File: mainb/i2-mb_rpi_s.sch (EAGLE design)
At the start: 36 parts, among them IC3 DS1307Z, T1 BC337, T2 BC337, X9 eth (mb->rpi)

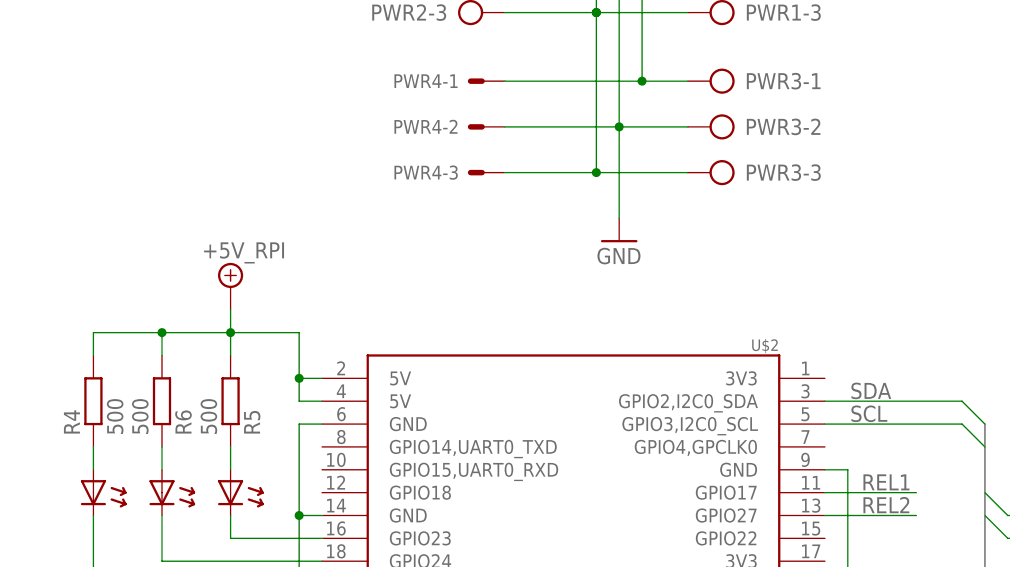
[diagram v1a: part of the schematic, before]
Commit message: mainb: 8) leds -> 3V3
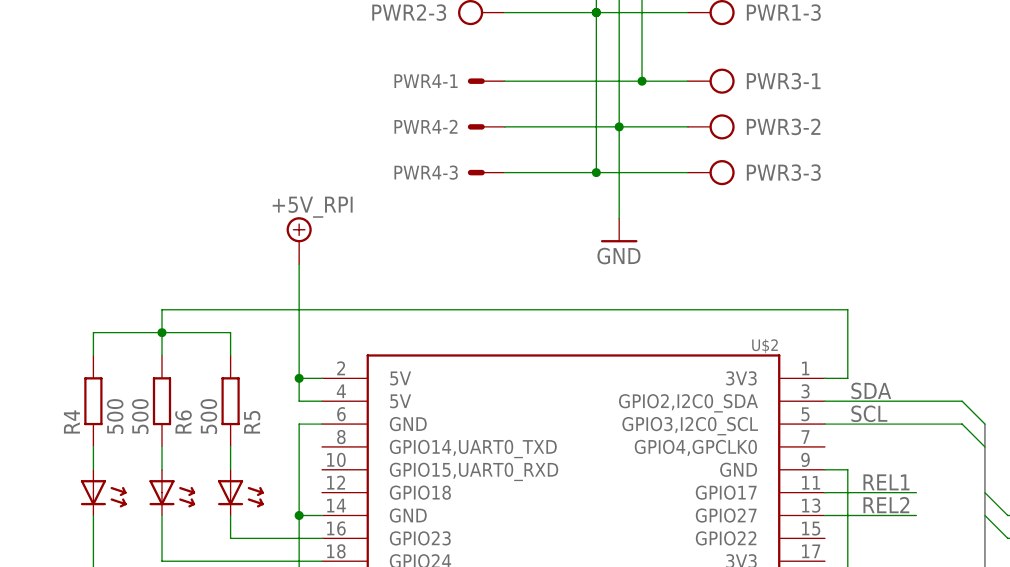
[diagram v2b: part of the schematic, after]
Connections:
- new net N$11: R4.2, R5.2, R6.2, U$2.3V3@1
- net +5V_RPI: no longer R4.2, R5.2, R6.2
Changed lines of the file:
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@@
 <instance part="X9" gate="-7" x="-182.88" y="40.64" rot="MR0"/>
 <instance part="X9" gate="-8" x="-182.88" y="38.1" rot="MR0"/>
-<instance part="SUPPLY2" gate="G$1" x="-71.12" y="20.32"/>
+<instance part="SUPPLY2" gate="G$1" x="-63.5" y="25.4"/>
 <instance part="SUPPLY3" gate="G$1" x="-91.44" y="-55.88" smashed="yes" rot="MR0">
 <attribute name="VALUE" x="-83.693" y="-52.451" size="1.778" layer="96" rot="MR0"/>
@@
 <wire x1="-60.96" y1="10.16" x2="-63.5" y2="10.16" width="0.1524" layer="91"/>
 <junction x="-63.5" y="10.16"/>
-<wire x1="-63.5" y1="10.16" x2="-63.5" y2="15.24" width="0.1524" layer="91"/>
-<wire x1="-63.5" y1="15.24" x2="-71.12" y2="15.24" width="0.1524" layer="91"/>
-<wire x1="-71.12" y1="15.24" x2="-71.12" y2="17.78" width="0.1524" layer="91"/>
+<wire x1="-63.5" y1="10.16" x2="-63.5" y2="22.86" width="0.1524" layer="91"/>
 <pinref part="SUPPLY2" gate="G$1" pin="+5V/1"/>
-<pinref part="R5" gate="G$1" pin="2"/>
-<pinref part="R6" gate="G$1" pin="2"/>
-<wire x1="-71.12" y1="12.7" x2="-71.12" y2="15.24" width="0.1524" layer="91"/>
-<wire x1="-78.74" y1="12.7" x2="-78.74" y2="15.24" width="0.1524" layer="91"/>
-<wire x1="-78.74" y1="15.24" x2="-71.12" y2="15.24" width="0.1524" layer="91"/>
-<junction x="-71.12" y="15.24"/>
-<pinref part="R4" gate="G$1" pin="2"/>
-<wire x1="-86.36" y1="12.7" x2="-86.36" y2="15.24" width="0.1524" layer="91"/>
-<wire x1="-86.36" y1="15.24" x2="-78.74" y2="15.24" width="0.1524" layer="91"/>
-<junction x="-78.74" y="15.24"/>
 </segment>
 <segment>
@@
 </segment>
 </net>
+<net name="N$11" class="0">
+<segment>
+<pinref part="R6" gate="G$1" pin="2"/>
+<wire x1="-78.74" y1="12.7" x2="-78.74" y2="15.24" width="0.1524" layer="91"/>
+<pinref part="R4" gate="G$1" pin="2"/>
+<wire x1="-86.36" y1="12.7" x2="-86.36" y2="15.24" width="0.1524" layer="91"/>
+<wire x1="-86.36" y1="15.24" x2="-78.74" y2="15.24" width="0.1524" layer="91"/>
+<pinref part="R5" gate="G$1" pin="2"/>
+<wire x1="-78.74" y1="15.24" x2="-71.12" y2="15.24" width="0.1524" layer="91"/>
+<wire x1="-71.12" y1="15.24" x2="-71.12" y2="12.7" width="0.1524" layer="91"/>
+<pinref part="U$2" gate="G$1" pin="3V3@1"/>
+<wire x1="-5.08" y1="10.16" x2="-2.54" y2="10.16" width="0.1524" layer="91"/>
+<wire x1="-2.54" y1="10.16" x2="-2.54" y2="17.78" width="0.1524" layer="91"/>
+<wire x1="-2.54" y1="17.78" x2="-78.74" y2="17.78" width="0.1524" layer="91"/>
+<wire x1="-78.74" y1="17.78" x2="-78.74" y2="15.24" width="0.1524" layer="91"/>
+<junction x="-78.74" y="15.24"/>
+</segment>
+</net>

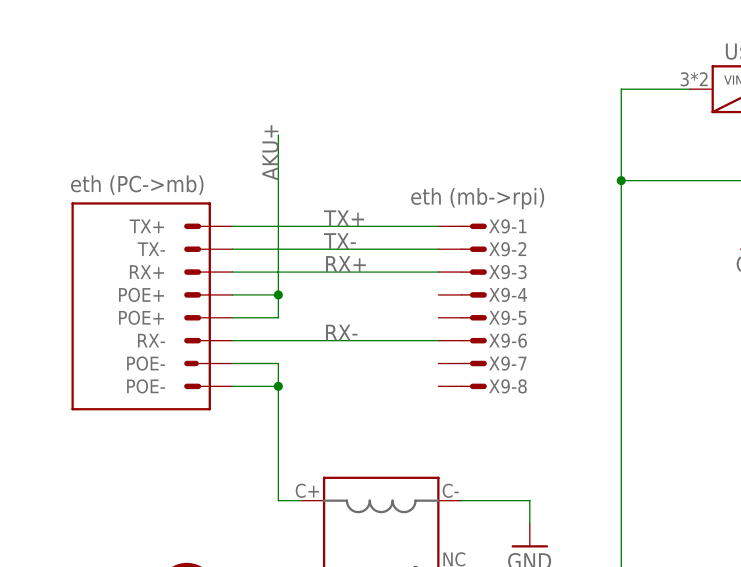
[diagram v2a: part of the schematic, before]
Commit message: mainb: 7) eth. conn. order
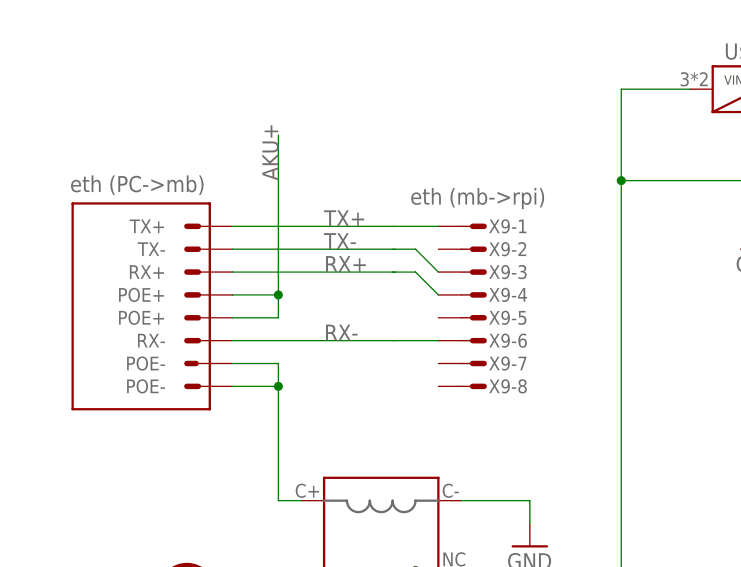
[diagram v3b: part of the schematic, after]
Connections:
- net RX+: now also X9-4.S; no longer X9-3.S
- net TX-: now also X9-3.S; no longer X9-2.S
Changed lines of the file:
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@@
 <label x="-200.66" y="55.88" size="1.778" layer="95"/>
 <pinref part="X_ETH" gate="G$1" pin="TX+"/>
-<wire x1="-187.96" y1="55.88" x2="-210.82" y2="55.88" width="0.1524" layer="91"/>
+<wire x1="-192.786" y1="55.88" x2="-193.04" y2="55.88" width="0.1524" layer="91"/>
 <pinref part="X9" gate="-1" pin="S"/>
+<wire x1="-193.04" y1="55.88" x2="-210.82" y2="55.88" width="0.1524" layer="91"/>
+<wire x1="-187.96" y1="55.88" x2="-192.786" y2="55.88" width="0.1524" layer="91"/>
 </segment>
 </net>
@@
 <label x="-200.66" y="53.34" size="1.778" layer="95"/>
 <pinref part="X_ETH" gate="G$1" pin="TX-"/>
-<wire x1="-187.96" y1="53.34" x2="-210.82" y2="53.34" width="0.1524" layer="91"/>
-<pinref part="X9" gate="-2" pin="S"/>
+<wire x1="-192.786" y1="53.34" x2="-193.04" y2="53.34" width="0.1524" layer="91"/>
+<pinref part="X9" gate="-3" pin="S"/>
+<wire x1="-193.04" y1="53.34" x2="-210.82" y2="53.34" width="0.1524" layer="91"/>
+<wire x1="-187.96" y1="50.8" x2="-190.5" y2="53.34" width="0.1524" layer="91"/>
+<wire x1="-190.5" y1="53.34" x2="-192.786" y2="53.34" width="0.1524" layer="91"/>
 </segment>
 </net>
 <net name="RX+" class="0">
 <segment>
-<wire x1="-210.82" y1="50.8" x2="-187.96" y2="50.8" width="0.1524" layer="91"/>
+<wire x1="-210.82" y1="50.8" x2="-193.04" y2="50.8" width="0.1524" layer="91"/>
 <label x="-200.66" y="50.8" size="1.778" layer="95"/>
 <pinref part="X_ETH" gate="G$1" pin="RX+"/>
-<pinref part="X9" gate="-3" pin="S"/>
+<pinref part="X9" gate="-4" pin="S"/>
+<wire x1="-193.04" y1="50.8" x2="-192.786" y2="50.8" width="0.1524" layer="91"/>
+<wire x1="-192.786" y1="50.8" x2="-190.5" y2="50.8" width="0.1524" layer="91"/>
+<wire x1="-190.5" y1="50.8" x2="-187.96" y2="48.26" width="0.1524" layer="91"/>
 </segment>
 </net>
@@
 <label x="-200.66" y="43.18" size="1.778" layer="95"/>
 <pinref part="X_ETH" gate="G$1" pin="RX-"/>
-<wire x1="-187.96" y1="43.18" x2="-210.82" y2="43.18" width="0.1524" layer="91"/>
+<wire x1="-192.786" y1="43.18" x2="-193.04" y2="43.18" width="0.1524" layer="91"/>
 <pinref part="X9" gate="-6" pin="S"/>
+<wire x1="-193.04" y1="43.18" x2="-210.82" y2="43.18" width="0.1524" layer="91"/>
+<wire x1="-192.786" y1="43.18" x2="-187.96" y2="43.18" width="0.1524" layer="91"/>
 </segment>
 </net>

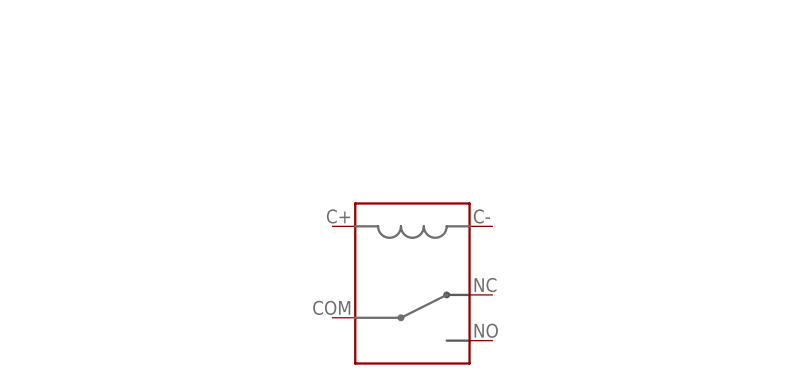
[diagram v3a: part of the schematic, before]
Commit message: mainb: 9) battery holder wholes dia
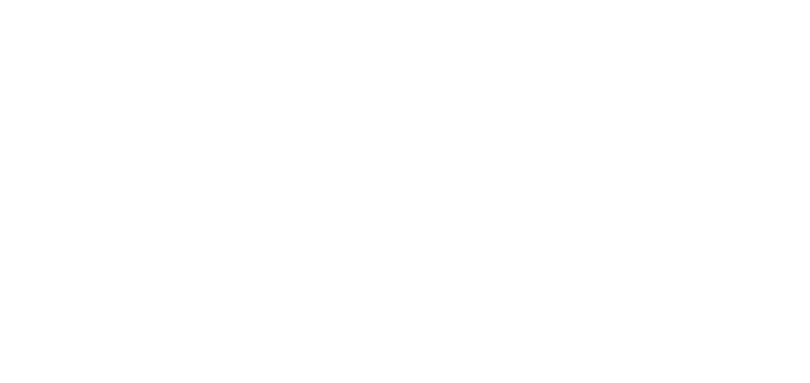
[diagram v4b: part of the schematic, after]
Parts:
- removed U$9: FBR51, wb:FBR51
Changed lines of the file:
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@@
 <part name="SUPPLY5" library="supply2" deviceset="+5V" device="" value="+5V_OUT"/>
 <part name="GND1" library="supply1" deviceset="GND" device=""/>
-<part name="U$9" library="wb" deviceset="FBR51" device=""/>
 </parts>
 <sheets>
@@
 </instance>
 <instance part="GND1" gate="1" x="40.64" y="-38.1"/>
-<instance part="U$9" gate="G$1" x="-187.96" y="-144.78"/>
 </instances>
 <busses>

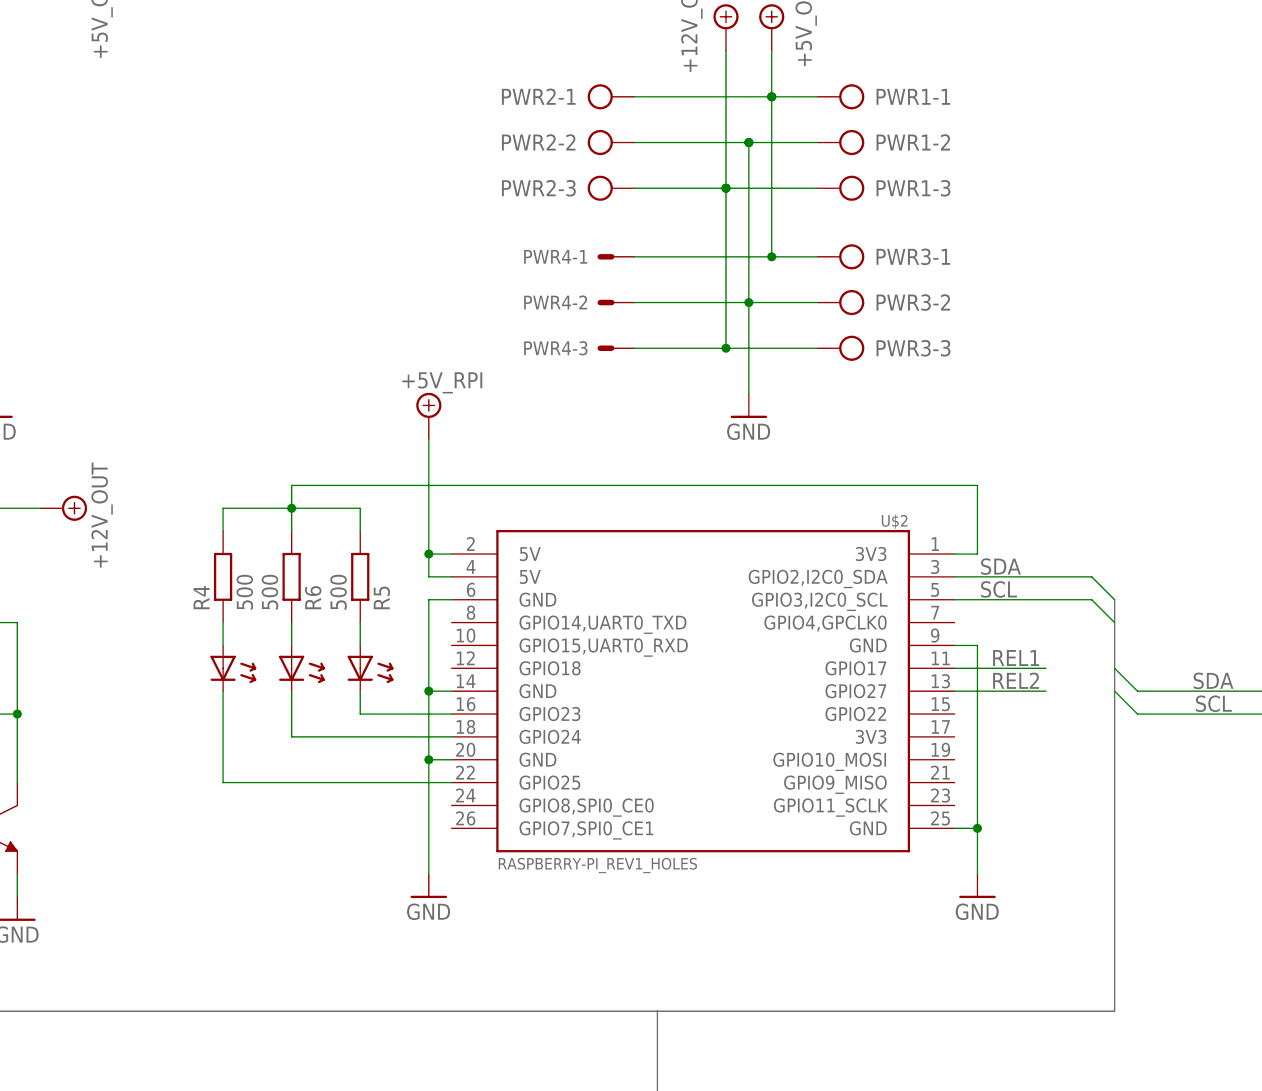
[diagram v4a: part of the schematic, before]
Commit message: mainb: 10) RPi UART for debugging
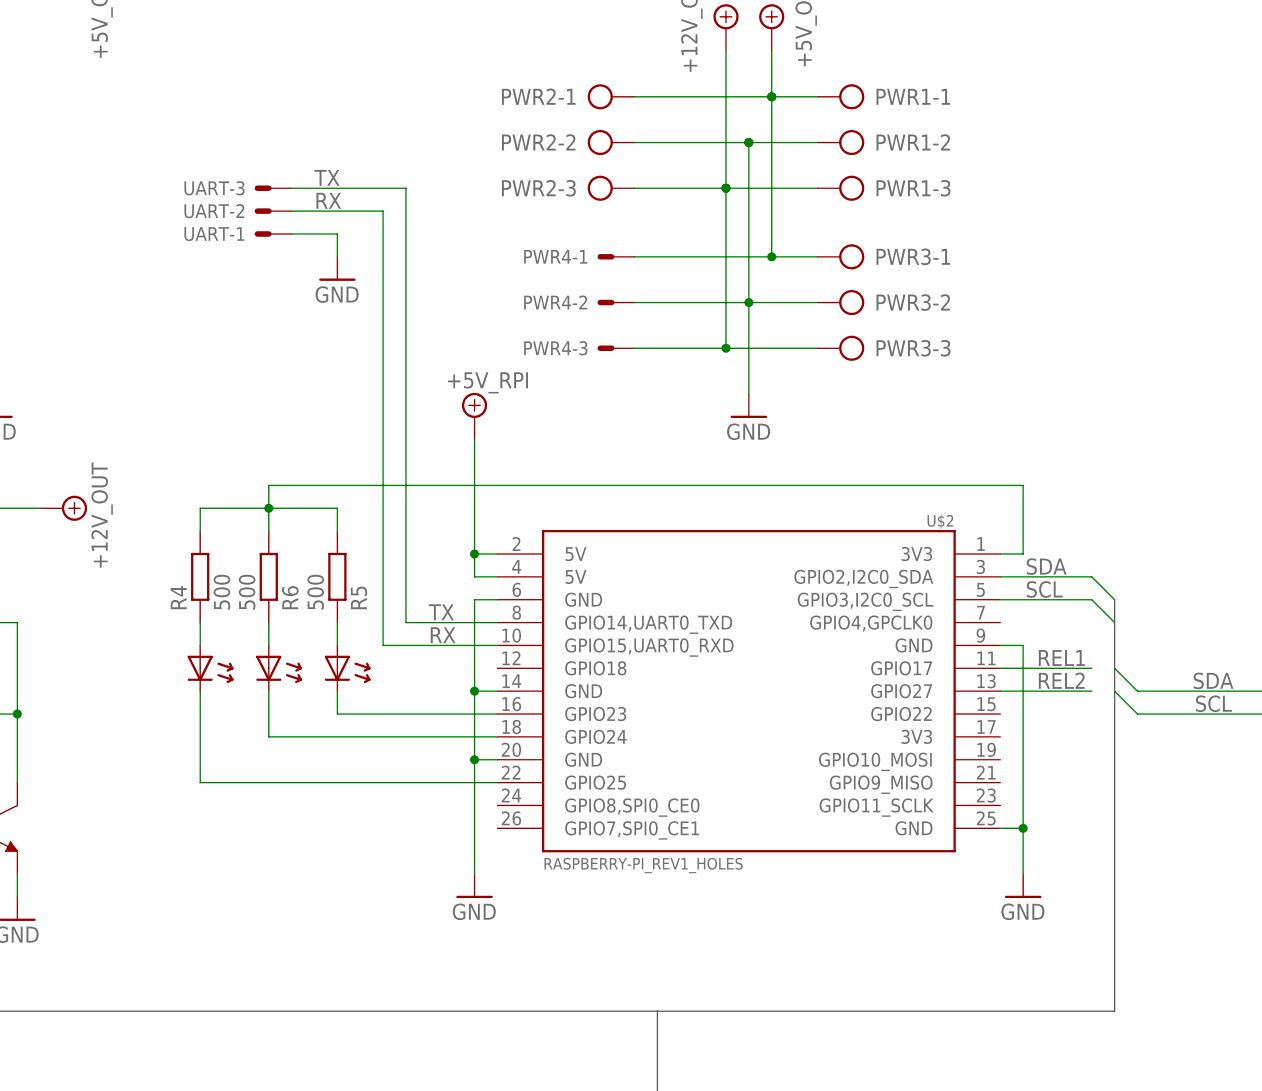
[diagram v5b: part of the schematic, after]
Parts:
- added UART: C-GRID-03-70543, con-molex:C-GRID-03-70543
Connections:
- new net RX: U$2.GPIO15,UART0_RXD, UART-2.S
- new net TX: U$2.GPIO14,UART0_TXD, UART-3.S
- net GND: now also UART-1.S
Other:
- moved on the sheet: R4, R5, R6, U$2

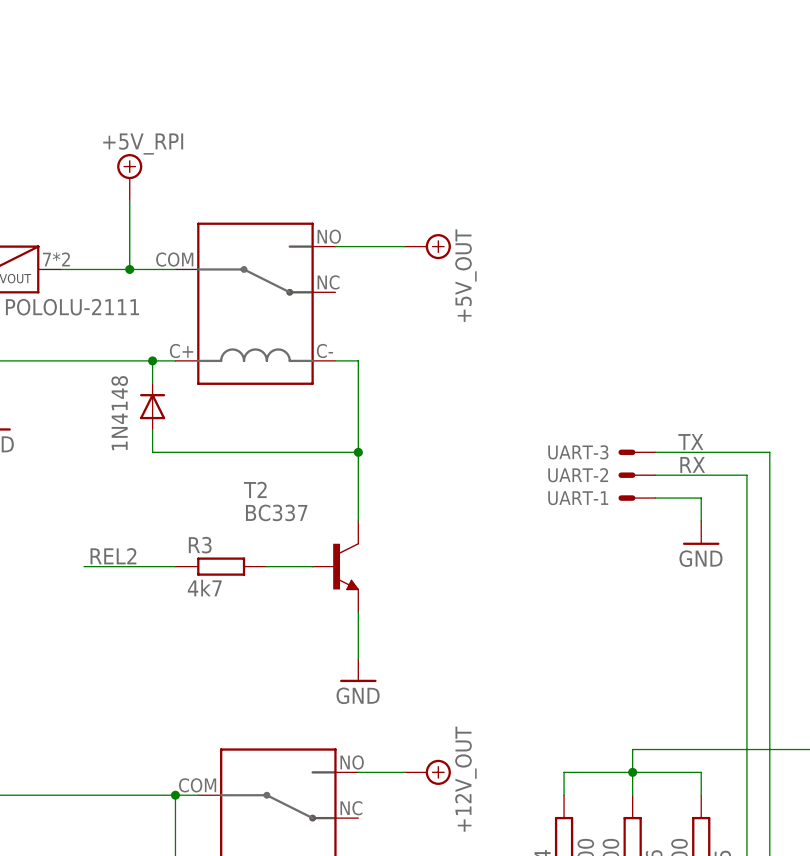
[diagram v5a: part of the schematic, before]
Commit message: trinocular/rpicam/ added
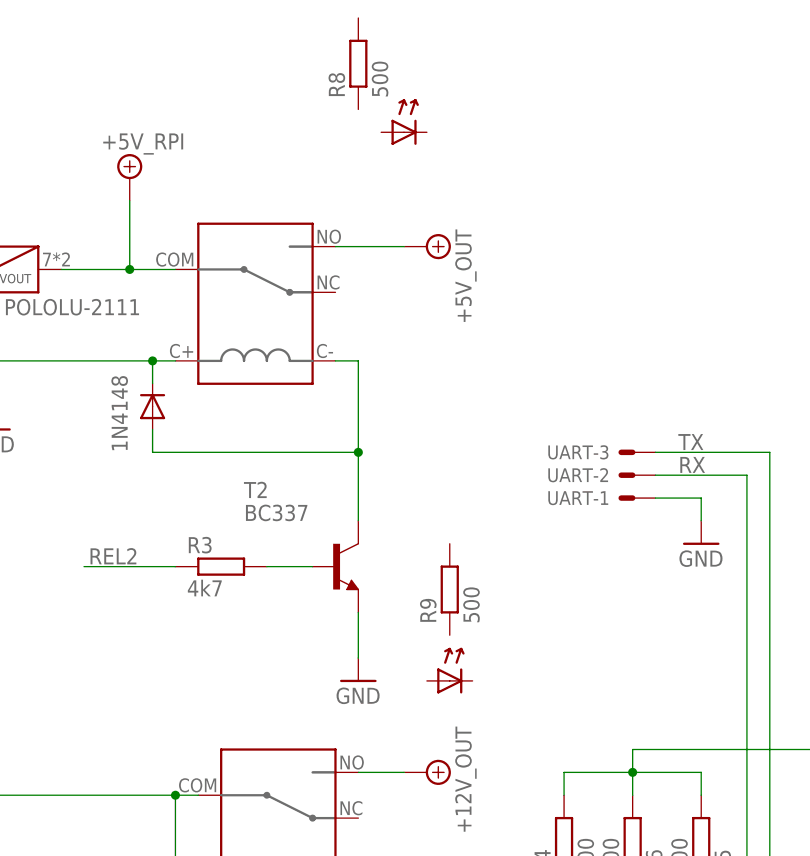
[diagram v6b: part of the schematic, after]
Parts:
- added LED4, LED5: LED0603, wb:LED0603
- added R8, R9: 500, rcl:R-EU_R0603
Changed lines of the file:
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@@
 <part name="UART" library="con-molex" deviceset="C-GRID-03" device="-70543"/>
 <part name="GND5" library="supply1" deviceset="GND" device=""/>
+<part name="LED4" library="wb" deviceset="LED0603" device="" value=""/>
+<part name="R8" library="rcl" deviceset="R-EU_" device="R0603" value="500"/>
+<part name="LED5" library="wb" deviceset="LED0603" device="" value=""/>
+<part name="R9" library="rcl" deviceset="R-EU_" device="R0603" value="500"/>
 </parts>
 <sheets>
@@
 <instance part="UART" gate="-3" x="-81.28" y="50.8" rot="R180"/>
 <instance part="GND5" gate="1" x="-73.66" y="40.64"/>
+<instance part="LED4" gate="G$1" x="-106.68" y="86.36" smashed="yes">
+<attribute name="VALUE" x="-104.14" y="84.0486" size="1.778" layer="96"/>
+</instance>
+<instance part="R8" gate="G$1" x="-111.76" y="93.98" rot="R90"/>
+<instance part="LED5" gate="G$1" x="-101.6" y="25.4" smashed="yes">
+<attribute name="VALUE" x="-99.06" y="23.0886" size="1.778" layer="96"/>
+</instance>
+<instance part="R9" gate="G$1" x="-101.6" y="35.56" rot="R90"/>
 </instances>
 <busses>
